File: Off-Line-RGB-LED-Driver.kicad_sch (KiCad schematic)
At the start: 11 parts, among them P1 Conn_WallPlug_Earth

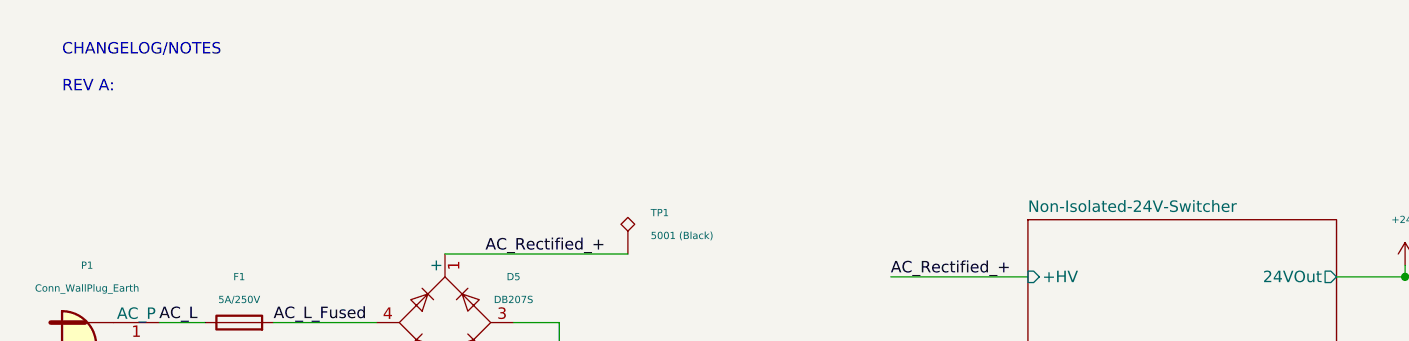
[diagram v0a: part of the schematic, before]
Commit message: [A02] Edited R4, R5
R4 20k -> 10k since nothing else uses 20k
R5 10k -> 510k to reduce D3 LED brightness
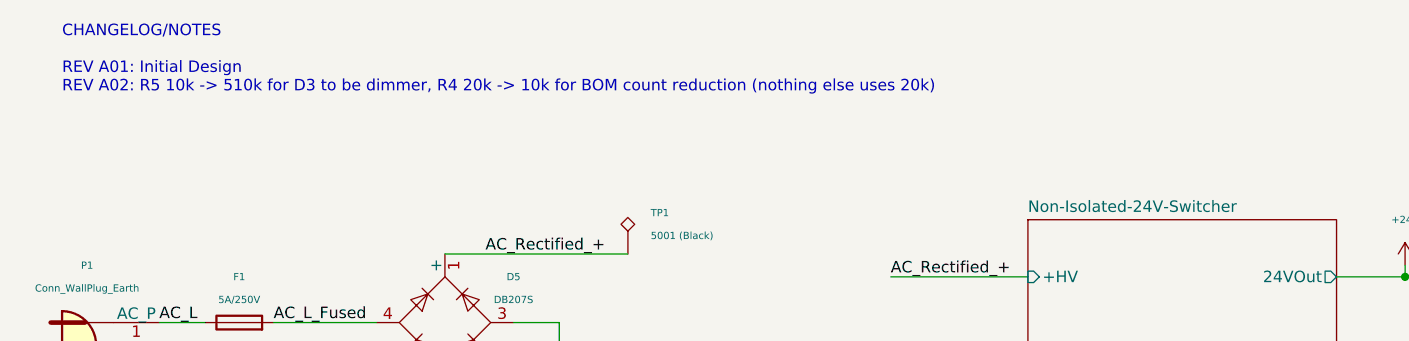
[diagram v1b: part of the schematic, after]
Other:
- note added: "CHANGELOG/NOTES REV A01: Initial Design REV A02: R5 10k -> 510k for D3 to be dimmer, R4 20k -> 10k for BOM count reduction (nothing else uses 20k)"
- note removed: "CHANGELOG/NOTES REV A:"
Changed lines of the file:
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@@
   (title_block
     (title "Main")
-    (date "2023-12-18")
-    (rev "A01")
+    (date "2023-12-30")
+    (rev "A02")
   )
   (junction (at 168.91 43.18) (diameter 0) (color 0 0 0 0)
@@
     (stroke (width 0) (type default))
   )
-  (text "CHANGELOG/NOTES\n\nREV A: " (at 19.685 22.86 0)
+  (text "CHANGELOG/NOTES\n\nREV A01: Initial Design\nREV A02: R5 10k -> 510k for D3 to be dimmer, R4 20k -> 10k for BOM count reduction (nothing else uses 20k)"
+    (at 19.685 22.86 0)
     (effects (font (size 1.27 1.27)) (justify left bottom))
   )
